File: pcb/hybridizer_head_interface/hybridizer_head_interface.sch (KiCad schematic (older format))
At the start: 116 parts, among them P1 HEADER_02X07_SMD, P2 HEADER_02X05_SMD, U1 HALL_DRV5053_OA_-73mT, U10 MAX4215, U11 HALL_DRV5053_OA_-73mT, U12 MAX4215, U13 HALL_DRV5053_OA_-73mT, U14 MAX4215, U15 DRV103, U16 DRV103, U17 DRV103, U18 DRV103, U19 DRV103, U2 MAX4215, U20 DRV103, U21 DRV103, U22 DRV103, U3 HALL_DRV5053_OA_-73mT, U4 MAX4215, U5 HALL_DRV5053_OA_-73mT, U6 MAX4215, U7 HALL_DRV5053_OA_-73mT, U8 MAX4215, U9 HALL_DRV5053_OA_-73mT

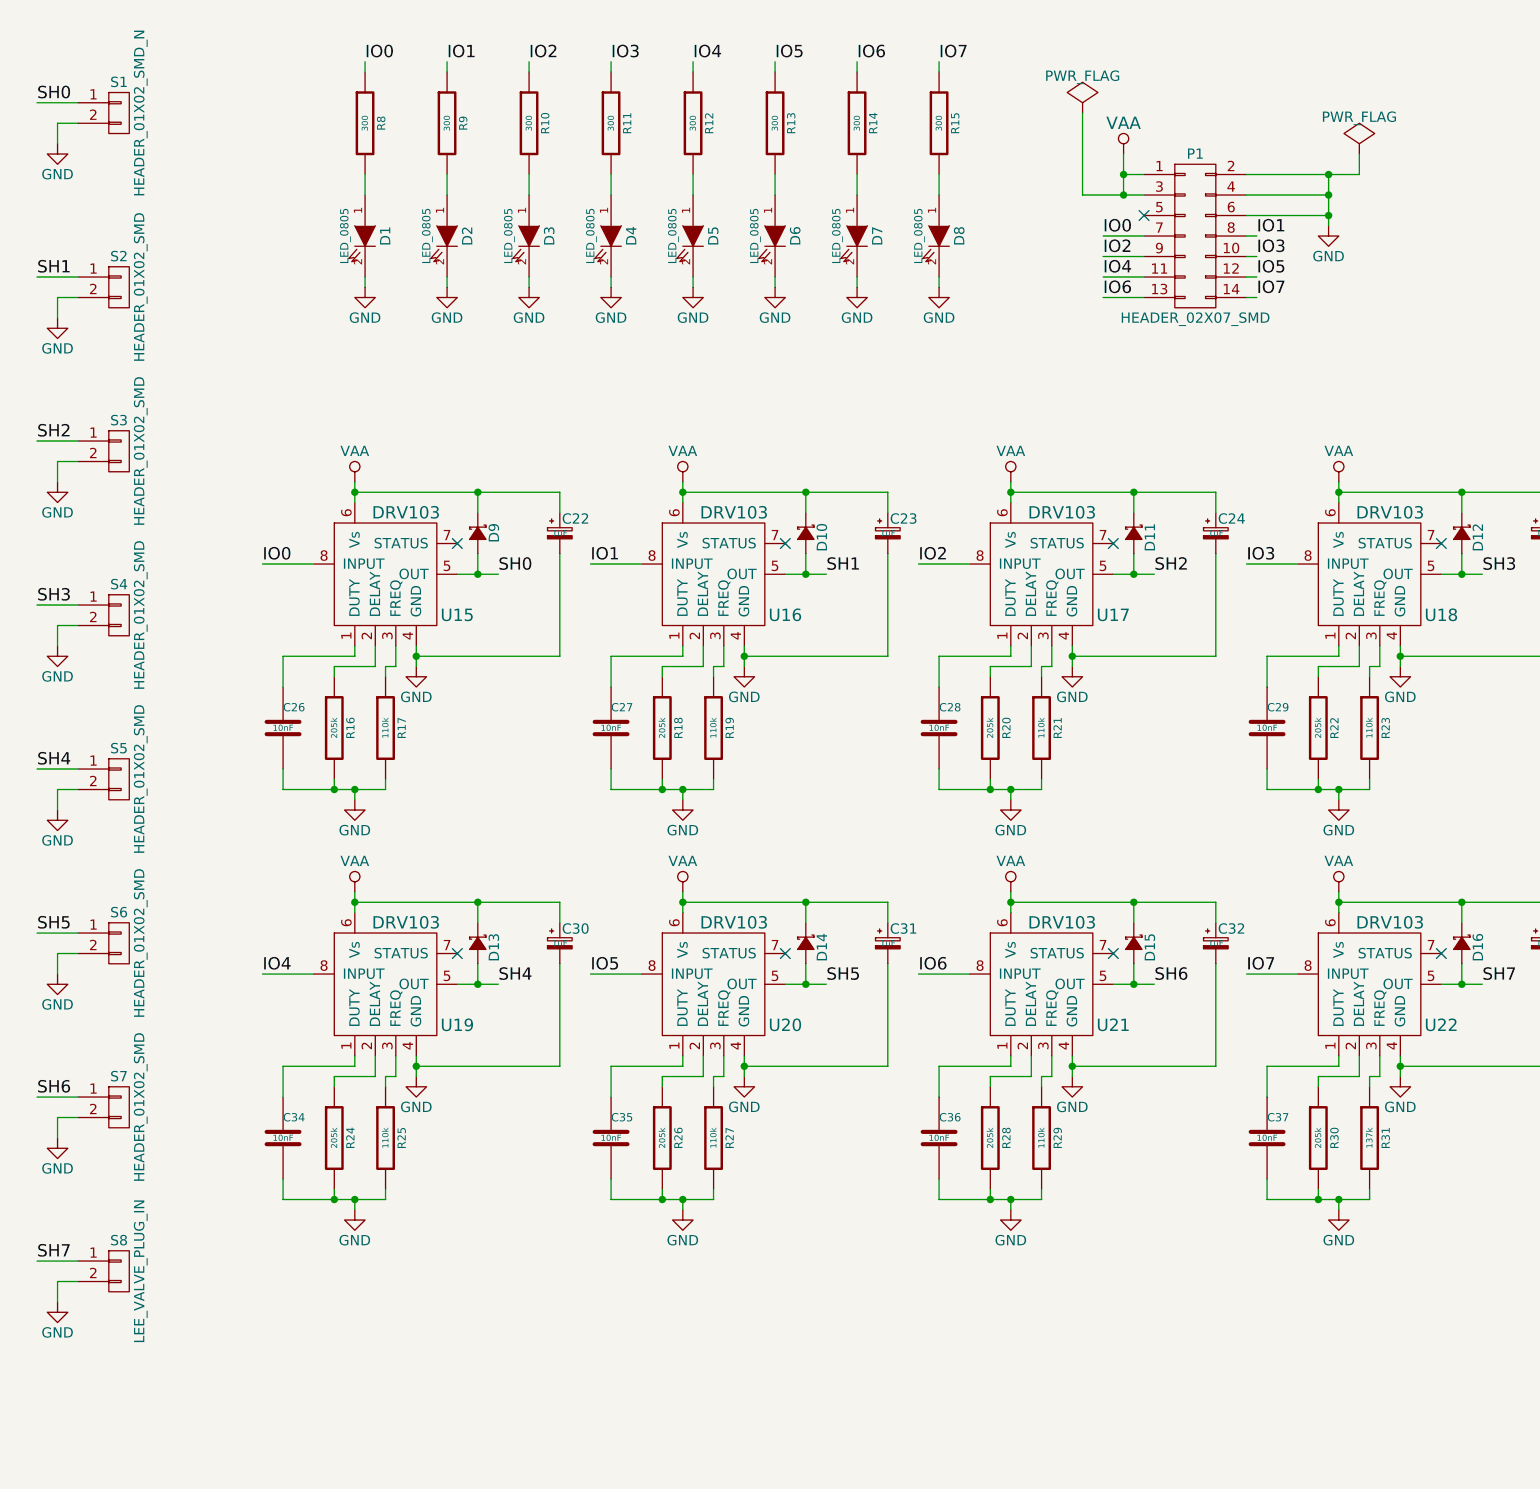
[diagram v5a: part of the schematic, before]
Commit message: Schematic changes towards hybridizer_head_interface v1.2.
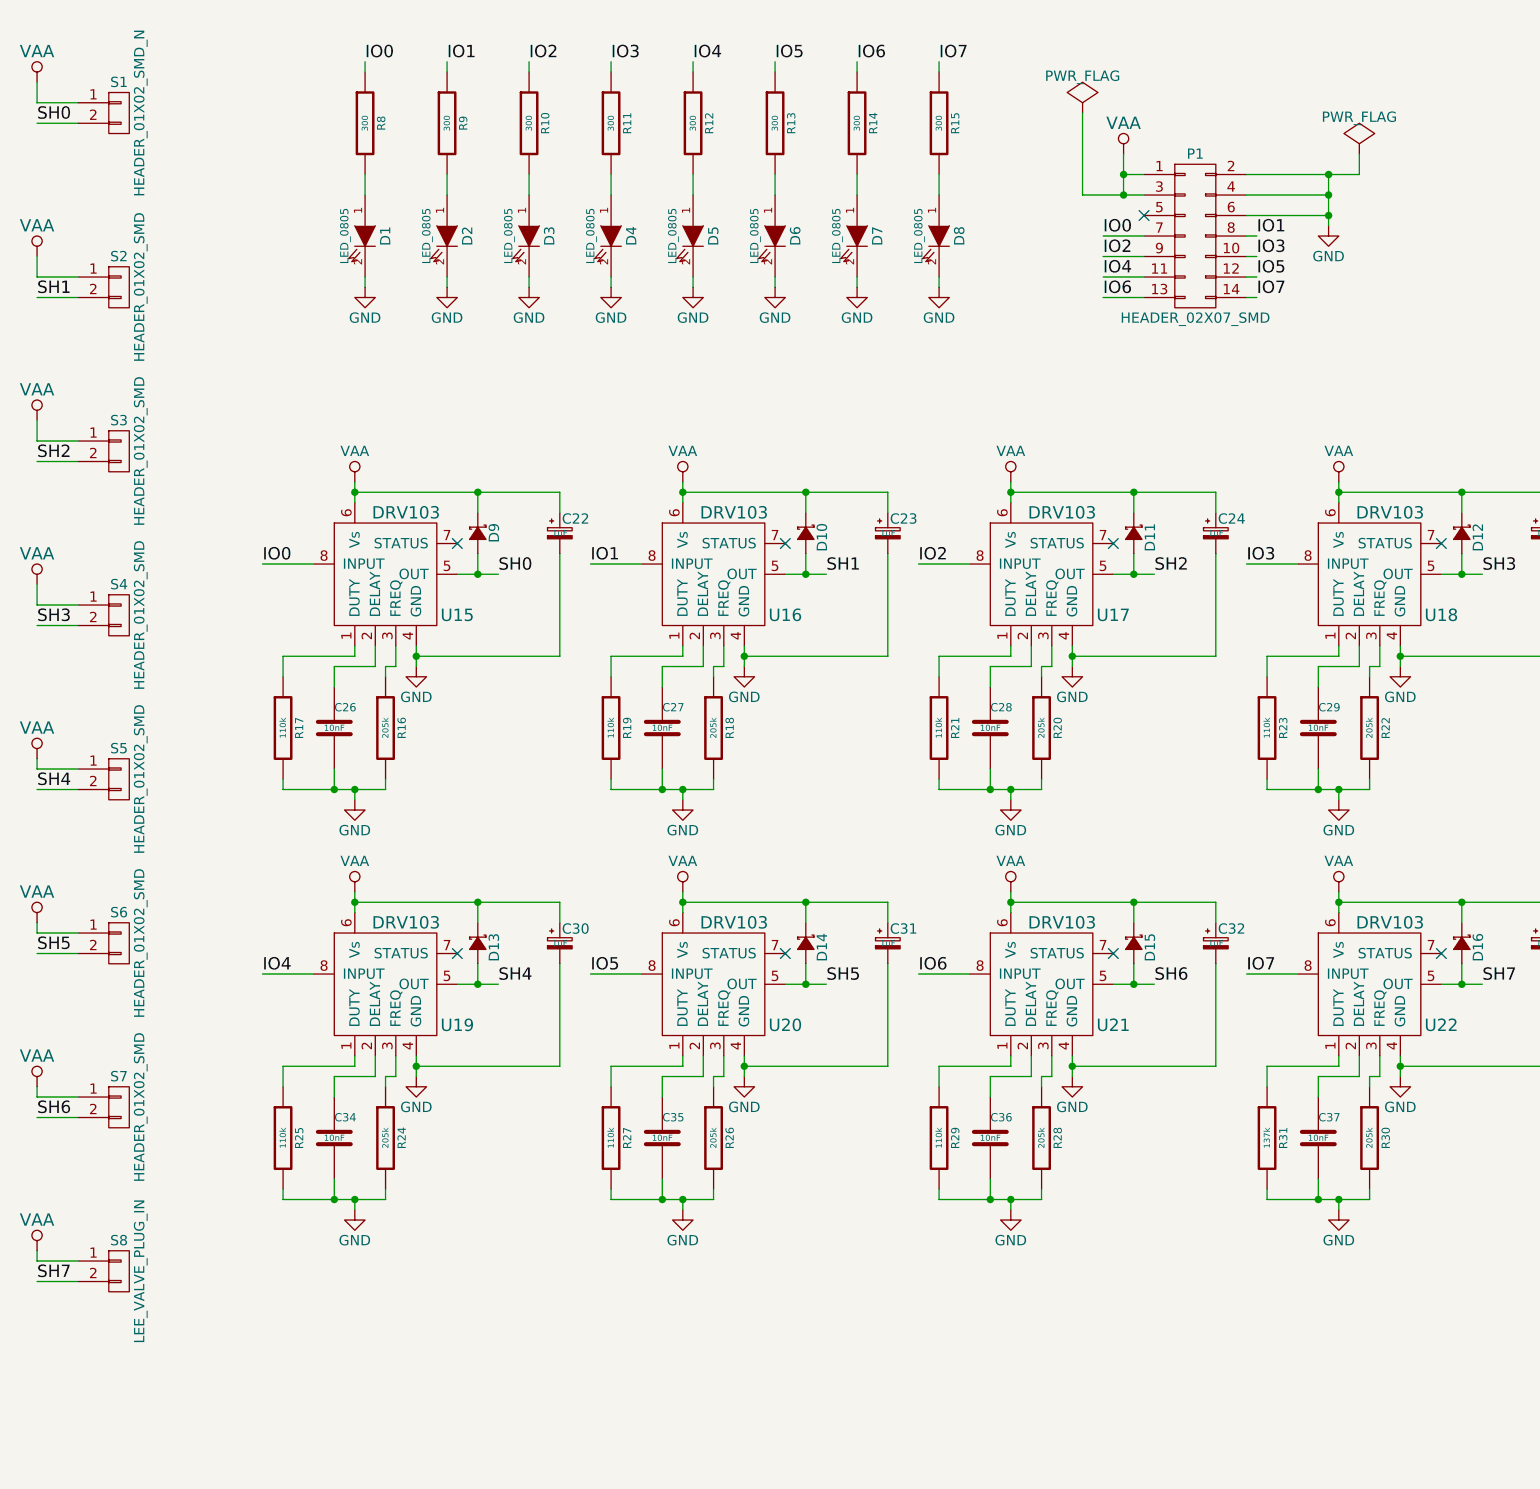
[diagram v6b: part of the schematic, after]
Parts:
- C22, C23, C24, C25, C30, C31, C32, C33: footprint hybridizer_head_interface:SM0805_POL -> hybridizer_head_interface:SM0805_POL_L
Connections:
- net GND: no longer S1.2 (P2), S2.2 (P2), S3.2 (P2), S4.2 (P2), S5.2 (P2), S6.2 (P2), S7.2 (P2), S8.2 (P2)
- net SH0: now also S1.2 (P2); no longer S1.1 (P1)
- net SH1: now also S2.2 (P2); no longer S2.1 (P1)
- net SH2: now also S3.2 (P2); no longer S3.1 (P1)
- net SH3: now also S4.2 (P2); no longer S4.1 (P1)
- net SH4: now also S5.2 (P2); no longer S5.1 (P1)
- net SH5: now also S6.2 (P2); no longer S6.1 (P1)
- net SH6: now also S7.2 (P2); no longer S7.1 (P1)
- net SH7: now also S8.2 (P2); no longer S8.1 (P1)
- net VAA: now also S1.1 (P1), S2.1 (P1), S3.1 (P1), S4.1 (P1), S5.1 (P1), S6.1 (P1), S7.1 (P1), S8.1 (P1)
- net at U15.1 (DUTY): now also R17.1; no longer C26.1
- net at U15.2 (DELAY): now also C26.1; no longer R16.1
- net at U15.3 (FREQ): now also R16.1; no longer R17.1
- net at U16.1 (DUTY): now also R19.1; no longer C27.1
- net at U16.2 (DELAY): now also C27.1; no longer R18.1
- net at U16.3 (FREQ): now also R18.1; no longer R19.1
- net at U17.1 (DUTY): now also R21.1; no longer C28.1
- net at U17.2 (DELAY): now also C28.1; no longer R20.1
- net at U17.3 (FREQ): now also R20.1; no longer R21.1
- net at U18.1 (DUTY): now also R23.1; no longer C29.1
- net at U18.2 (DELAY): now also C29.1; no longer R22.1
- net at U18.3 (FREQ): now also R22.1; no longer R23.1
- net at U19.1 (DUTY): now also R25.1; no longer C34.1
- net at U19.2 (DELAY): now also C34.1; no longer R24.1
- net at U19.3 (FREQ): now also R24.1; no longer R25.1
- net at U20.1 (DUTY): now also R27.1; no longer C35.1
- net at U20.2 (DELAY): now also C35.1; no longer R26.1
- net at U20.3 (FREQ): now also R26.1; no longer R27.1
- net at U21.1 (DUTY): now also R29.1; no longer C36.1
- net at U21.2 (DELAY): now also C36.1; no longer R28.1
- net at U21.3 (FREQ): now also R28.1; no longer R29.1
- net at U22.1 (DUTY): now also R31.1; no longer C37.1
- net at U22.2 (DELAY): now also C37.1; no longer R30.1
- net at U22.3 (FREQ): now also R30.1; no longer R31.1
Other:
- moved on the sheet: C26, C27, C28, C29, C34, C35, C36, C37, R16, R17, R18, R19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

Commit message: Progress towards hybridizer_head_interface_v1.2.
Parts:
- removed C11, C14, C17, C2, C20, C5, C8: 8.2nF, hybridizer_head_interface:SM1210, symbol 8.2nF
- removed C12, C15, C18, C21, C3, C6, C9: 0.1uF, hybridizer_head_interface:SM1210, symbol 0.1uF
- removed R1, R2, R3, R4, R5, R6, R7: 200k, hybridizer_head_interface:SM1210, symbol 200k
- removed U10, U12, U14, U2, U4, U6, U8: MAX4215, hybridizer_head_interface:SOIC_8_N, symbol MAX4215
- added C38, C39, C40, C41, C42, C43, C44: 0.1uF, hybridizer_head_interface:SM1210, symbol 0.1uF
- added C45, C47: 22uF, hybridizer_head_interface:SM1210_POL, symbol 22uF_1210_POL
- added C46, C48: 10uF, hybridizer_head_interface:SM1210, symbol 10uF
- added P3: HEADER_02X05_SMD, hybridizer_head_interface:HEADER_02x05_SMD, symbol HEADER_02X05_SMD
- added U1, U11, U13, U3, U5, U7, U9: VA, hybridizer_head_interface:SOT-23-3, symbol HALL_DRV5053_VA_-9mT
- U23: renamed from U1; value HALL_DRV5053_OA_-73mT -> OA
- U24: renamed from U3; value HALL_DRV5053_OA_-73mT -> OA
- U25: renamed from U5; value HALL_DRV5053_OA_-73mT -> OA
- U26: renamed from U7; value HALL_DRV5053_OA_-73mT -> OA
- U27: renamed from U9; value HALL_DRV5053_OA_-73mT -> OA
- U28: renamed from U11; value HALL_DRV5053_OA_-73mT -> OA
- U29: renamed from U13; value HALL_DRV5053_OA_-73mT -> OA
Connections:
- net +5V: now also C38.1, C39.1, C40.1, C41.1, C42.1, C43.1, C44.1, C47.1, C48.1, U1.1 (Vcc), U11.1 (Vcc), U13.1 (Vcc), U3.1 (Vcc), U5.1 (Vcc), U7.1 (Vcc), U9.1 (Vcc)
- net A0: now also U1.2 (OUT)
- net A1: now also U3.2 (OUT)
- net A2: now also U5.2 (OUT)
- net A3: now also U7.2 (OUT)
- net A4: now also U9.2 (OUT)
- net A5: now also U11.2 (OUT)
- net A6: now also U13.2 (OUT)
- net GND: now also C45.2, C46.2; no longer C1.2, C10.2, C13.2, C16.2, C19.2, C4.2, C7.2, U23.3 (GND), U24.3 (GND), U25.3 (GND), U26.3 (GND), U27.3 (GND), U28.3 (GND), U29.3 (GND)
- net VAA: now also C45.1, C46.1
- net GNDA: now reaches P2.2 (P2)
- net GNDA: now also C1.2, C10.2, C13.2, C16.2, C19.2, C4.2, C7.2, U23.3 (GND), U24.3 (GND), U25.3 (GND), U26.3 (GND), U27.3 (GND), U28.3 (GND), U29.3 (GND), C38.2, C39.2, C40.2, C41.2, C42.2, C43.2, C44.2, C47.2, C48.2, U1.3 (GND), U11.3 (GND), U13.3 (GND), U3.3 (GND), U5.3 (GND), U7.3 (GND), U9.3 (GND)
- net A10: now reaches U25.2 (OUT)
- net A10: now also P3.5 (P5)
- net A11: now reaches U26.2 (OUT)
- net A11: now also P3.6 (P6)
- net A12: now reaches U27.2 (OUT)
- net A12: now also P3.7 (P7)
- net A13: now reaches U28.2 (OUT)
- net A13: now also P3.8 (P8)
- net A14: now reaches U29.2 (OUT)
- net A14: now also P3.9 (P9)
- net A9: now reaches U24.2 (OUT)
- net A9: now also P3.4 (P4)
- net A8: now reaches U23.2 (OUT)
- net A8: now also P3.3 (P3)
- no-connect marks 11 -> 13
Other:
- moved on the sheet: P2, U23, U24, U25, U26, U27, U28, U29
